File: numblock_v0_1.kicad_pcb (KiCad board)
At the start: 2 copper layers, 100 x 100 mm, 137 parts, among them J1 Conn_01x14_Female, J2 Conn_01x14_Female, J3 Conn_01x05_Female, SW1 SW_PUSH-MX_W_LED, SW10 SW_PUSH-MX_W_LED, SW11 SW_PUSH-MX_W_LED, SW12 SW_PUSH-MX_W_LED, SW13 SW_PUSH-MX_W_LED, SW14 SW_PUSH-MX_W_LED, SW15 SW_PUSH-MX_W_LED, SW16 SW_PUSH-MX_W_LED, SW17 SW_PUSH-MX_W_LED, SW18 SW_PUSH-MX_W_LED, SW19 SW_PUSH-MX_W_LED, SW2 SW_PUSH-MX_W_LED, SW20 SW_PUSH-MX_W_LED, SW21 Rotary_Encoder_Switch, SW22 Rotary_Encoder_Switch, SW3 SW_PUSH-MX_W_LED, SW4 SW_PUSH-MX_W_LED, SW5 SW_PUSH-MX_W_LED, SW6 SW_PUSH-MX_W_LED, SW7 SW_PUSH-MX_W_LED, SW8 SW_PUSH-MX_W_LED, SW9 SW_PUSH-MX_W_LED

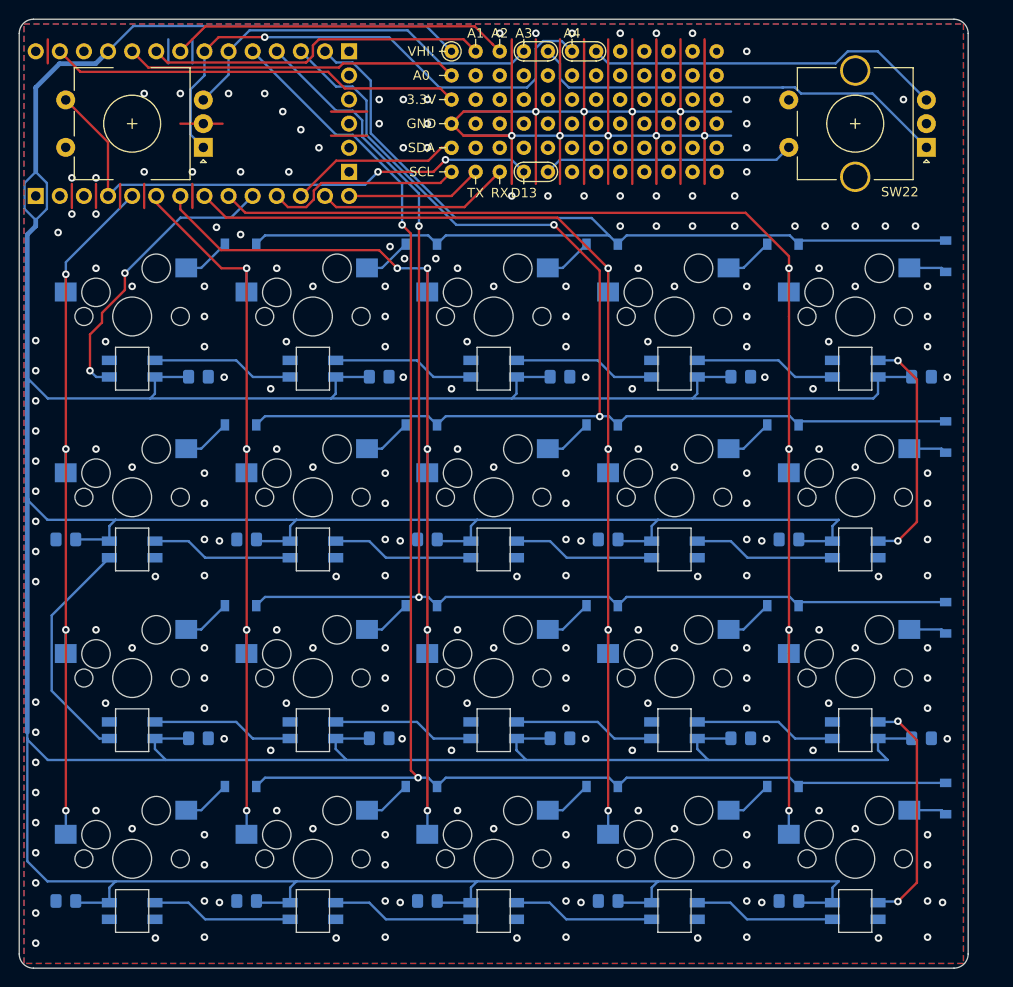
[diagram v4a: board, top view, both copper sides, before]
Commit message: added top led and oled display support
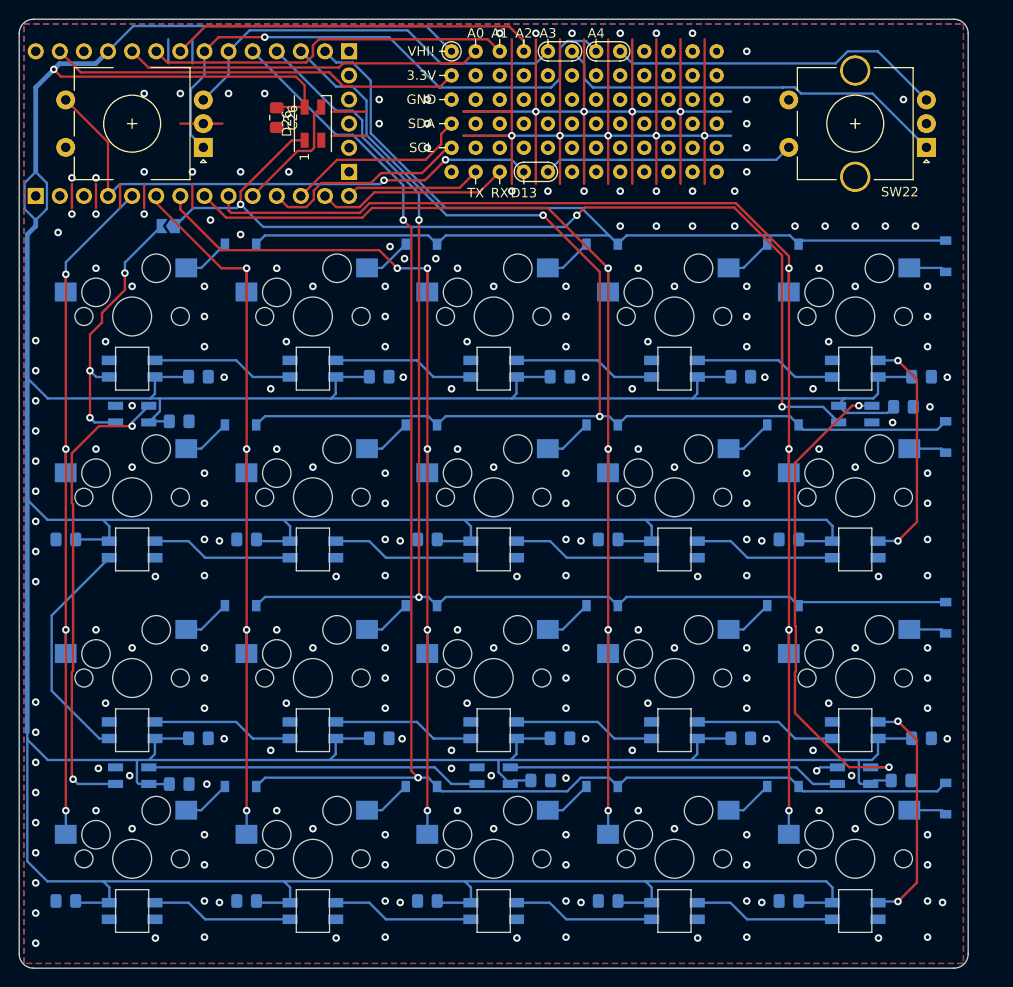
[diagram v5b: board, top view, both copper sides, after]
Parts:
- added C21: C, Capacitor_SMD:C_0805_2012Metric_Pad1.18x1.45mm_HandSolder, B.Cu at (119.4, 66.7)
- added C22: C, Capacitor_SMD:C_0805_2012Metric_Pad1.18x1.45mm_HandSolder, B.Cu at (119.1, 106.0)
- added C23: C, Capacitor_SMD:C_0805_2012Metric_Pad1.18x1.45mm_HandSolder, B.Cu at (43.1, 106.4)
- added C24: C, Capacitor_SMD:C_0805_2012Metric_Pad1.18x1.45mm_HandSolder, B.Cu at (43.1, 68.2)
- added C25: C, Capacitor_SMD:C_0805_2012Metric_Pad1.18x1.45mm_HandSolder, B.Cu at (81.2, 106.0)
- added C26: C, Capacitor_SMD:C_0805_2012Metric_Pad1.18x1.45mm_HandSolder, F.Cu at (53.3, 36.2)
- added D21: SK6812MINI, LED_SMD:LED_SK6812MINI_PLCC4_3.5x3.5mm_P1.75mm, B.Cu at (114.3, 67.4)
- added D22: SK6812MINI, LED_SMD:LED_SK6812MINI_PLCC4_3.5x3.5mm_P1.75mm, B.Cu at (114.2, 105.5)
- added D23: SK6812MINI, LED_SMD:LED_SK6812MINI_PLCC4_3.5x3.5mm_P1.75mm, B.Cu at (76.2, 105.5)
- added D24: SK6812MINI, LED_SMD:LED_SK6812MINI_PLCC4_3.5x3.5mm_P1.75mm, B.Cu at (38.1, 105.5)
- added D25: SK6812MINI, LED_SMD:LED_SK6812MINI_PLCC4_3.5x3.5mm_P1.75mm, B.Cu at (38.1, 67.4)
- added D26: SK6812MINI, LED_SMD:LED_SK6812MINI_PLCC4_3.5x3.5mm_P1.75mm, F.Cu at (57.1, 36.8)
- added JP1: Jumper_2_Open, Jumper:SolderJumper-2_P1.3mm_Open_TrianglePad1.0x1.5mm, B.Cu at (41.9, 47.6)
- moved REF** 21.8 mm to (71.8, 41.9)
- moved H7 3.59 mm to (74.3, 29.2)
- moved H13 2.54 mm to (81.9, 29.2)
- moved H15 2.54 mm to (79.4, 29.2)
- moved H9 2.54 mm to (87.0, 29.2)
- moved H1 2.54 mm to (71.8, 34.3)
- moved H2 2.54 mm to (71.8, 31.8)
- moved H3 2.54 mm to (71.8, 36.8)
- moved H4 2.54 mm to (71.8, 39.4)
- moved H10 2.54 mm to (84.5, 29.2)
- moved H14 2.54 mm to (89.5, 29.2)
- moved H8 2.54 mm to (76.8, 29.2)
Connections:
- SW1 pad 3: /LED -> /leds/backlight
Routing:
- net /leds/led_pin: track 0.00 -> 101.8 mm, vias 0 -> 3
- net +5V: track 614.6 -> 671.7 mm, vias 0 -> 1
- net Net-(D21-Pad1): track 0.00 -> 51.3 mm, vias 0 -> 2
- net Net-(D24-Pad1): track 0.00 -> 49.6 mm, vias 0 -> 2
- net Net-(D23-Pad1): track 0.00 -> 35.3 mm
- net Net-(D22-Pad1): track 0.00 -> 35.2 mm
- net /leds/backlight: track 0.00 -> 28.5 mm, vias 0 -> 3
- net /LED: track 31.0 -> 13.2 mm, vias 2 -> 0
- net GND: track 239.7 -> 235.9 mm, vias 240 -> 247
- net /A2: track 35.8 -> 39.0 mm
- net /Rot1: track 57.3 -> 59.9 mm
- net /Rot2: track 40.2 -> 42.8 mm
- net /A0: track 35.1 -> 37.6 mm
- net Net-(H14-Pad1): track 38.0 -> 35.4 mm
- net Net-(H10-Pad1): track 45.0 -> 42.5 mm
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
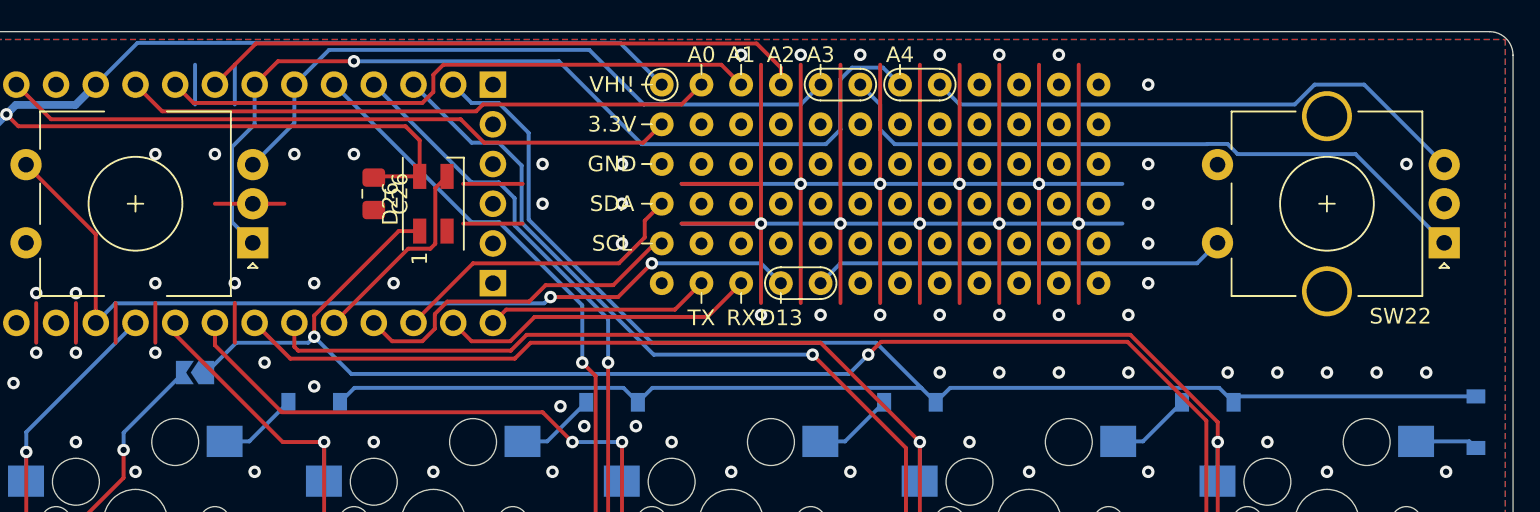
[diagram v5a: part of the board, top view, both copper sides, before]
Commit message: fixed display position
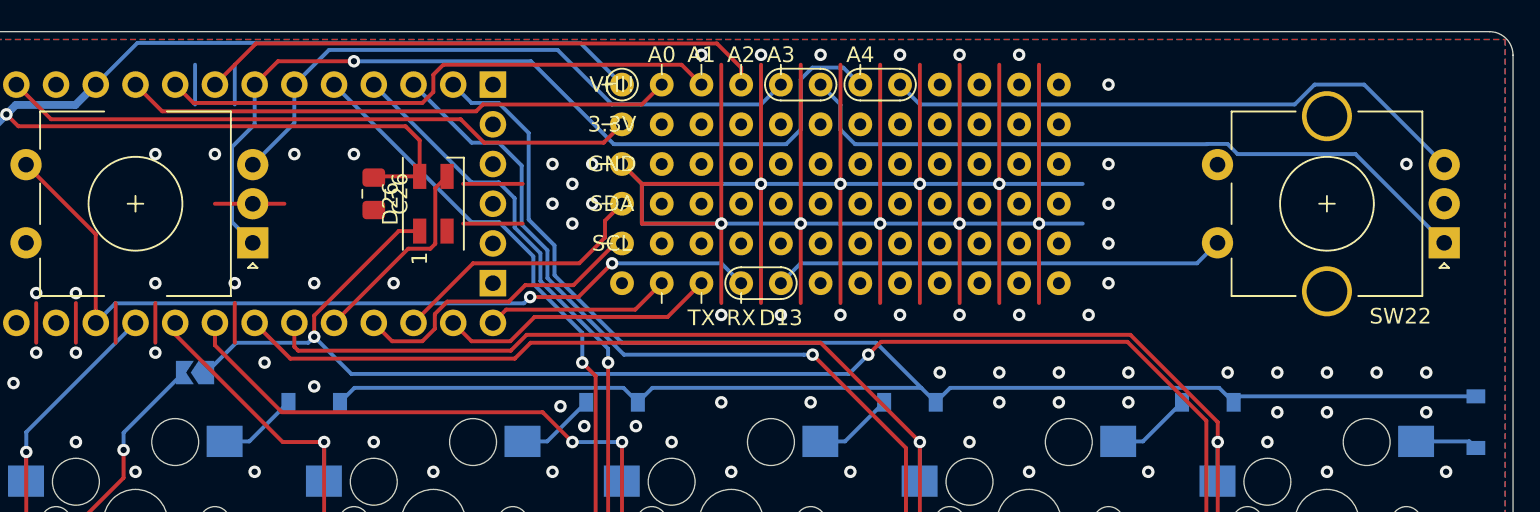
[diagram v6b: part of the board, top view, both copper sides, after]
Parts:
- removed the REF** at (99.7, 41.9)
- removed the REF** at (99.7, 39.4)
- removed the REF** at (99.7, 36.8)
- removed the REF** at (99.7, 31.8)
- removed the REF** at (99.7, 34.3)
- removed the REF** at (99.7, 29.2)
- removed the REF** at (71.8, 41.9)
- removed the REF** at (71.8, 29.2)
- added REF**: hole_30mil, sofle RGB:hole_30mil, F.Cu at (81.9, 41.9)
- added REF**: hole_30mil, sofle RGB:hole_30mil, F.Cu at (71.8, 39.4)
- added REF**: hole_30mil, sofle RGB:hole_30mil, F.Cu at (89.5, 29.2)
- added REF**: hole_30mil, sofle RGB:hole_30mil, F.Cu at (69.2, 41.9)
- added REF**: hole_30mil, sofle RGB:hole_30mil, F.Cu at (69.2, 29.2)
- added REF**: hole_30mil, sofle RGB:hole_30mil, F.Cu at (71.8, 34.3)
- added REF**: hole_30mil, sofle RGB:hole_30mil, F.Cu at (71.8, 36.8)
- added REF**: hole_30mil, sofle RGB:hole_30mil, F.Cu at (71.8, 31.8)
- moved H11 2.54 mm to (79.4, 41.9)
- moved H12 2.54 mm to (76.8, 41.9)
- moved H13 2.54 mm to (79.4, 29.2)
- moved H15 2.54 mm to (76.8, 29.2)
- moved H5 2.54 mm to (71.8, 41.9)
- moved H7 2.54 mm to (71.8, 29.2)
- moved H9 2.54 mm to (84.5, 29.2)
- moved H1 2.54 mm to (69.2, 34.3)
- moved H10 2.54 mm to (81.9, 29.2)
- moved H14 2.54 mm to (87.0, 29.2)
- moved H2 2.54 mm to (69.2, 31.8)
- moved H3 2.54 mm to (69.2, 36.8)
- moved H4 2.54 mm to (69.2, 39.4)
- moved H6 2.54 mm to (74.3, 41.9)
- moved H8 2.54 mm to (74.3, 29.2)
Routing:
- net GND: track 235.9 -> 244.6 mm, vias 247 -> 256
- net +5V: track 671.7 -> 669.2 mm
- net /A0: track 37.6 -> 35.1 mm
- net Net-(H11-Pad1): track 26.5 -> 29.0 mm
- net /SW: track 57.9 -> 55.3 mm
- net /Rot2: track 42.8 -> 40.2 mm
- net /Rot1: track 59.9 -> 57.3 mm
- net /A2: track 39.0 -> 36.5 mm
- net /RX: track 14.4 -> 11.8 mm
- net Net-(H14-Pad1): track 35.4 -> 38.0 mm
- net /TX: track 20.4 -> 17.9 mm
- net Net-(H10-Pad1): track 42.5 -> 45.0 mm
- net /SDA: track 19.7 -> 17.1 mm
- net /SCL: track 22.0 -> 19.5 mm
- net /A1: track 38.9 -> 36.3 mm
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
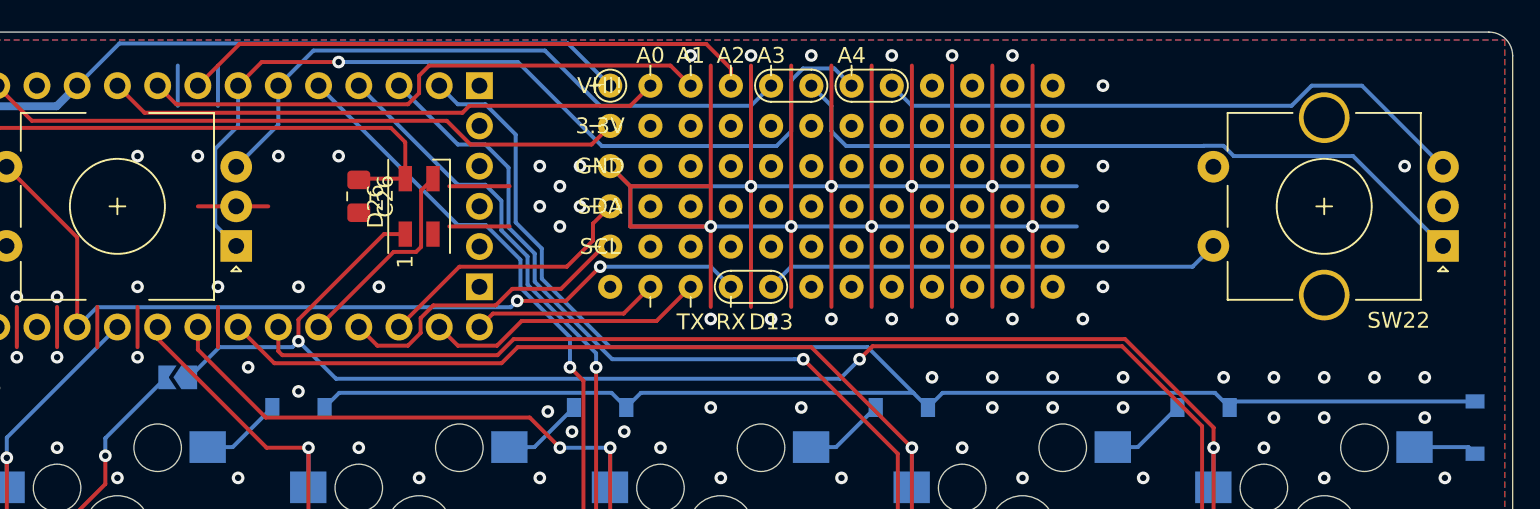
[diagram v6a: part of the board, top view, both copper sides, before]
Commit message: moved display down
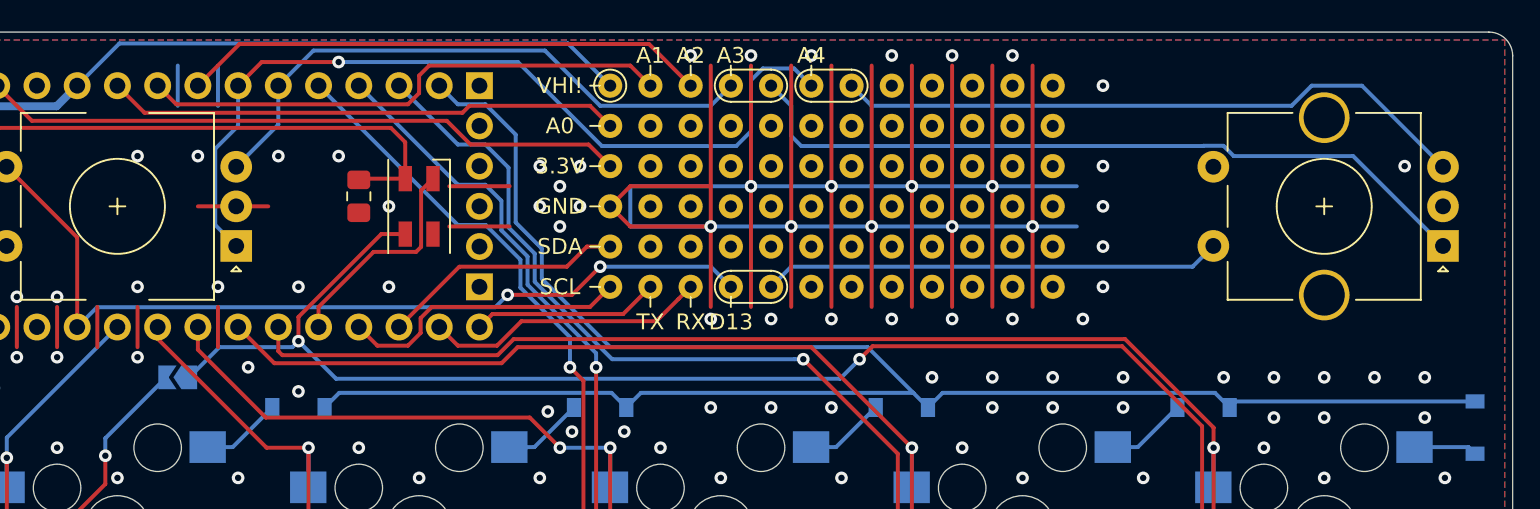
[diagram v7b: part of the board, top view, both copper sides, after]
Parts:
- moved REF** 21.8 mm to (87.0, 29.2)
- moved H7 3.59 mm to (69.2, 31.8)
- moved H10 2.54 mm to (79.4, 29.2)
- moved H13 2.54 mm to (76.8, 29.2)
- moved H14 2.54 mm to (84.5, 29.2)
- moved H8 2.54 mm to (71.8, 29.2)
- moved H1 2.54 mm to (69.2, 36.8)
- moved H2 2.54 mm to (69.2, 34.3)
- moved H3 2.54 mm to (69.2, 39.4)
- moved H4 2.54 mm to (69.2, 41.9)
- moved H15 2.54 mm to (74.3, 29.2)
- moved H9 2.54 mm to (81.9, 29.2)
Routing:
- net /A2: track 36.5 -> 33.3 mm
- net Net-(H10-Pad1): track 45.0 -> 47.7 mm
- net GND: track 244.6 -> 242.0 mm, vias 256 -> 258
- net /Rot2: track 40.2 -> 37.7 mm
- net /A1: track 36.3 -> 33.8 mm
- net Net-(H14-Pad1): track 38.0 -> 40.5 mm
- net /Rot1: track 57.3 -> 54.8 mm
- net /A0: track 35.1 -> 32.5 mm
- net /SDA: track 17.1 -> 15.4 mm
- net /SCL: track 19.5 -> 18.4 mm
- net /LED: track 13.2 -> 13.9 mm

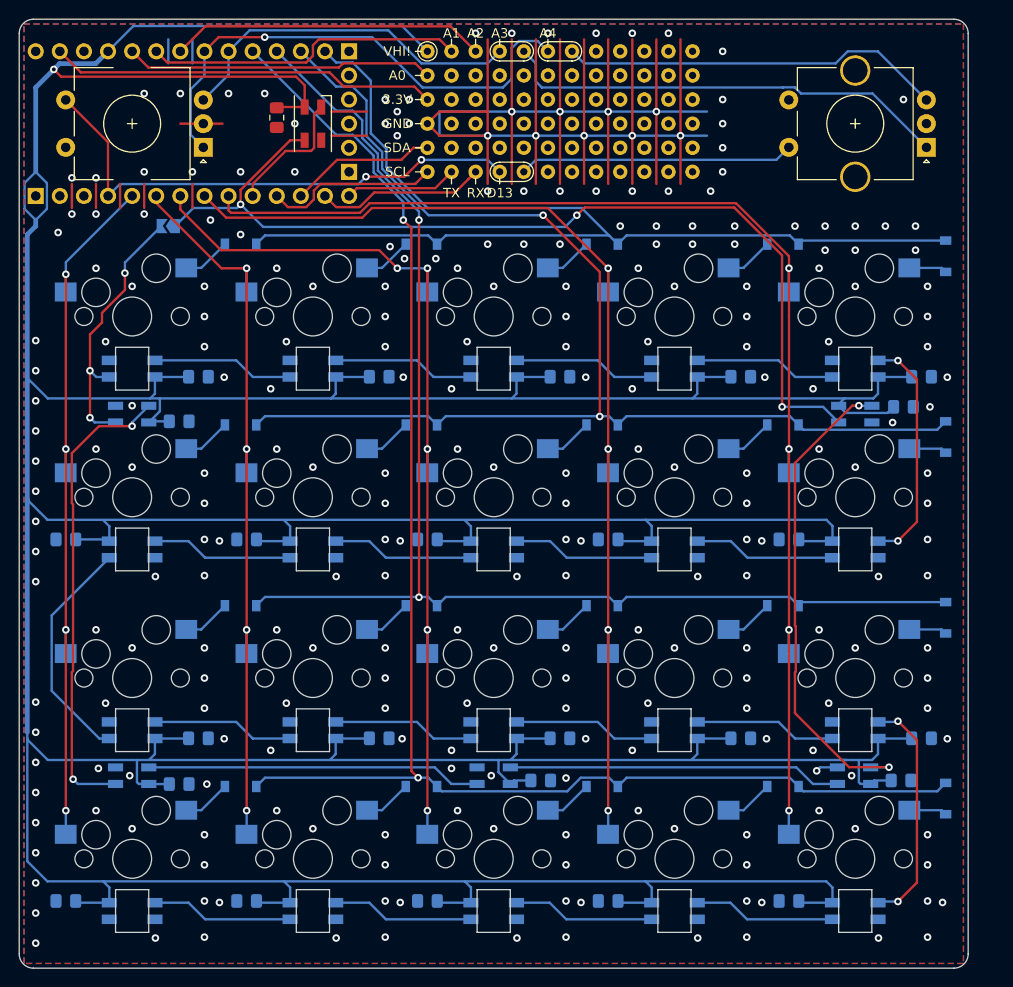
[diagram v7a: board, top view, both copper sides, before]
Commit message: fixed backlight leds; added holes
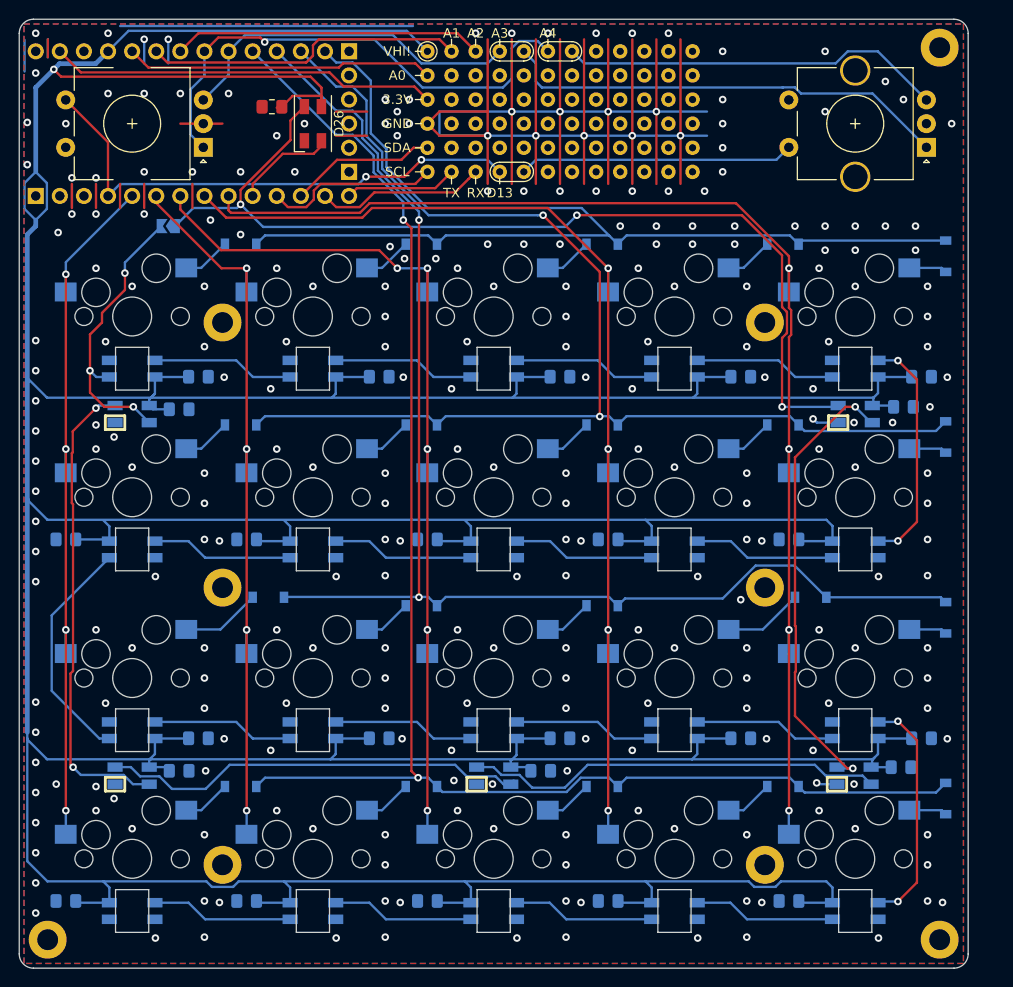
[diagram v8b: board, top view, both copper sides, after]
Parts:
- added TH1: HOLE, sofle:M2_HOLE_PCB, F.Cu at (104.8, 85.7)
- added TH1: HOLE, sofle:M2_HOLE_PCB, F.Cu at (47.6, 85.7)
- added TH1: HOLE, sofle:M2_HOLE_PCB, F.Cu at (47.6, 57.8)
- added TH1: HOLE, sofle:M2_HOLE_PCB, F.Cu at (104.8, 57.8)
- added TH1: HOLE, sofle:M2_HOLE_PCB, F.Cu at (104.8, 114.9)
- added TH1: HOLE, sofle:M2_HOLE_PCB, F.Cu at (47.6, 114.9)
- added TH1: HOLE, sofle:M2_HOLE_PCB, F.Cu at (29.2, 122.8)
- added TH1: HOLE, sofle:M2_HOLE_PCB, F.Cu at (123.2, 122.8)
- added TH1: HOLE, sofle:M2_HOLE_PCB, F.Cu at (123.2, 28.8)
- D21, D22, D23, D24, D25, D26: footprint LED_SMD:LED_SK6812MINI_PLCC4_3.5x3.5mm_P1.75mm -> sofle RGB:LED_SK6812MINI_HS
- moved D11 3.05 mm to (52.5, 86.7)
- moved D14 3.05 mm to (109.6, 86.7)
- moved C22 1.40 mm to (119.1, 104.6)
- moved C23 1.40 mm to (43.1, 105.0)
- moved C24 1.27 mm to (43.1, 66.9)
- moved C26 1.25 mm to (52.8, 35.1), turned to 180 degrees
- moved C25 1.02 mm to (81.2, 105.0)
- turned D22 to 180 degrees
- turned D23 to 180 degrees
- turned D24 to 180 degrees
- turned D25 to 180 degrees
- turned D26 to 270 degrees
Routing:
- net GND: track 242.0 -> 281.8 mm, vias 258 -> 268
- net Net-(D23-Pad1): track 35.3 -> 45.1 mm
- net Net-(D22-Pad1): track 35.2 -> 44.3 mm
- net +5V: track 669.2 -> 660.1 mm
- net Net-(D11-Pad1): track 5.12 -> 8.40 mm
- net Net-(D14-Pad1): track 5.12 -> 8.40 mm
- net /LED: track 13.9 -> 10.7 mm
- net Net-(D21-Pad1): track 51.3 -> 48.5 mm
- net /leds/backlight: track 28.5 -> 30.5 mm
- net /leds/led_pin: track 101.9 -> 103.8 mm
- net /R3: track 139.9 -> 139.0 mm
- net Net-(D24-Pad1): track 49.6 -> 50.2 mm
- net /A2: track 33.3 -> 32.7 mm
